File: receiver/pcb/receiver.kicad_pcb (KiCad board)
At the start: 4 copper layers, 41 x 41 mm, 25 parts, among them U1 RZ7886, U2 RZ7886, U3 XIAO ESP32C3

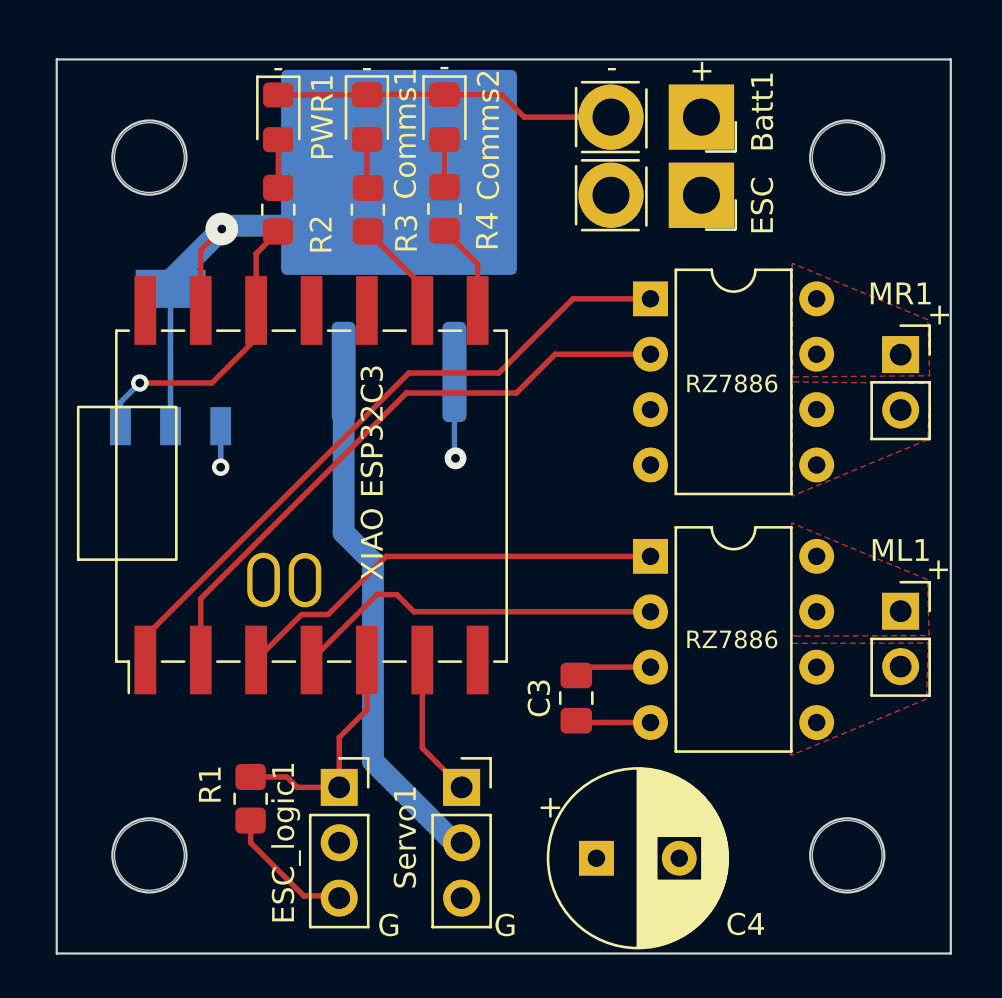
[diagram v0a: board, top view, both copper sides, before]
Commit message: fixed mistakenly small motor pads in receiver V6.
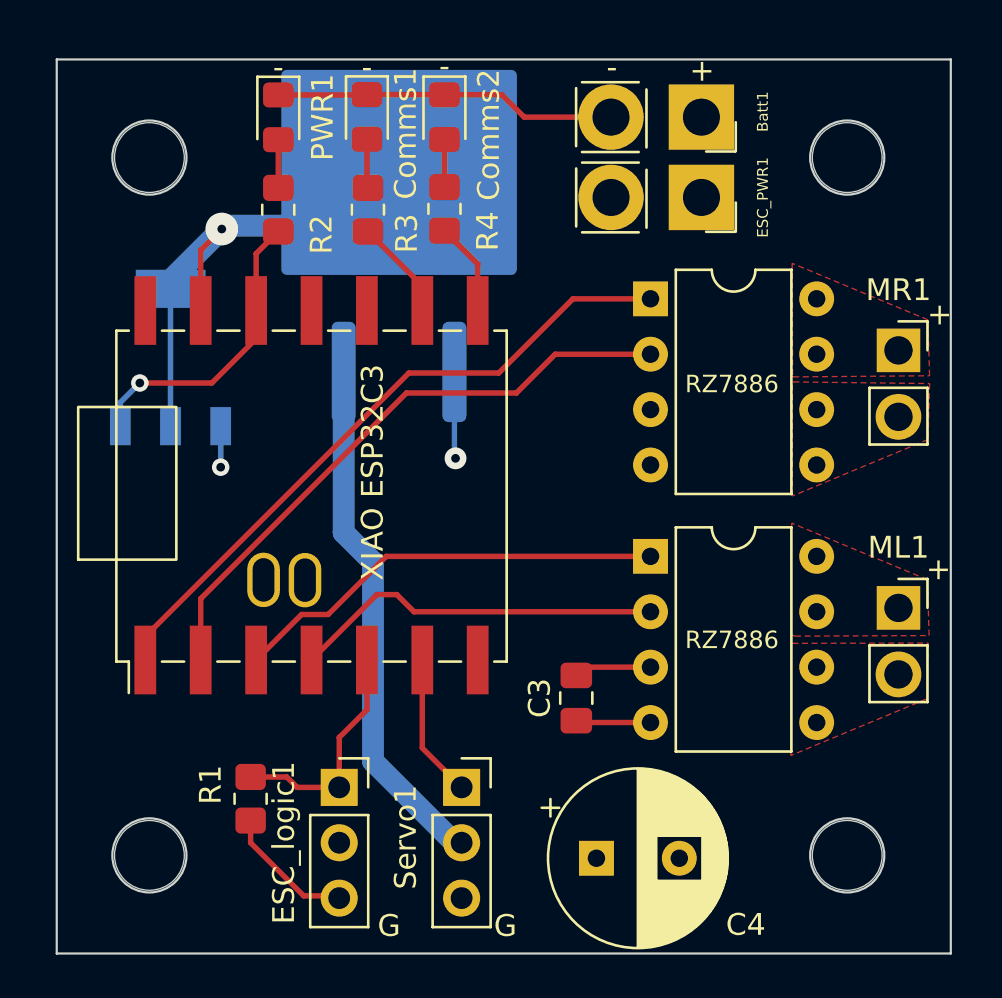
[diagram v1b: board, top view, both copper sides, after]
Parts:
- removed ESC: Conn_01x02_Female, custom:battery_pads
- added ESC_PWR1: Conn_01x02_Female, custom:battery_pads, F.Cu at (174.8, 84.8)
- ML1: footprint Connector_PinSocket_2.54mm:PinSocket_1x02_P2.54mm_Vertical -> custom:DC_motor_output
- MR1: value Conn_01x02_Female -> motor_output; footprint Connector_PinSocket_2.54mm:PinSocket_1x02_P2.54mm_Vertical -> custom:DC_motor_output
- moved MR1 0.22 mm to (185.1, 91.8)
- moved ML1 0.18 mm to (185.1, 103.7)
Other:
- board text added: "VS Receiver V7"
- board text removed: "VS Receiver V6"

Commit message: V8 as ordered from jlcpcb. Order #: Y34-2569843A
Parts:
- removed C3: .1 uF, Capacitor_SMD:C_0805_2012Metric_Pad1.18x1.45mm_HandSolder
- removed C4: 470 uF, Capacitor_THT:CP_Radial_D8.0mm_P3.80mm
- removed L7806: L7806, Package_TO_SOT_SMD:TO-263-2_TabPin1
- removed U2: RZ7886, Package_DIP:DIP-8_W7.62mm
- removed U3: XIAO ESP32C3, XIAO_ESP32C3:xiao_esp32c3
- added C1: 270 uF, Capacitor_THT:CP_Radial_D8.0mm_P3.80mm, F.Cu at (170.0, 114.7)
- added C2: 100nF, Capacitor_SMD:C_0805_2012Metric_Pad1.18x1.45mm_HandSolder, F.Cu at (167.9, 83.6)
- added IC1: L7806CD2T-TR, L7806CD2T-TR:TO254P1542X460-3N, B.Cu at (162.3, 87.7)
- added ML2: VNH7100BASTR, VNH7100BASTR:SOIC127P600X175-16N, F.Cu at (179.3, 105.4)
- added ML_selector1: ML_selector, Connector_PinSocket_2.54mm:PinSocket_1x03_P2.54mm_Vertical, F.Cu at (172.2, 106.1)
- added MR2: VNH7100BASTR, VNH7100BASTR:SOIC127P600X175-16N, F.Cu at (179.3, 92.5)
- added MR_selector1: MR_selector, Connector_PinSocket_2.54mm:PinSocket_1x03_P2.54mm_Vertical, F.Cu at (172.6, 95.5)
- U1: value RZ7886 -> XIAO ESP32C3; footprint Package_DIP:DIP-8_W7.62mm -> XIAO_ESP32C3:xiao_esp32c3
- moved U1 15.9 mm to (160.0, 97.5), turned to 90 degrees
- moved MR1 1.04 mm to (185.3, 90.8)
- moved ML1 0.39 mm to (185.5, 103.5)
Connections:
- R3 pad 1: Net-(U3-D8) -> Net-(U1-D8)
- R4 pad 1: Net-(U3-D7) -> Net-(U1-D6)
- U1 pad 3: GND -> Net-(ML2-INB)
- U1 pad 4: +12V -> Net-(ML2-INA)
- U1 pad 5: Net-(MR1-Pin_2) -> Net-(ESC_logic1-Pin_1)
- U1 pad 6: Net-(MR1-Pin_2) -> Net-(Servo1-Pin_1)
- U1 pad 7: Net-(MR1-Pin_1) -> Net-(U1-D6)
- U1 pad 8: Net-(MR1-Pin_1) -> /MR_PWM
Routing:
- net Net-(U1-D6): track 0.00 -> 72.9 mm
- net /ML_PWM: track 0.00 -> 33.7 mm, vias 0 -> 2
- net Net-(ML2-INB): track 0.00 -> 26.9 mm
- net /MR_sense: track 0.00 -> 25.6 mm, vias 0 -> 2
- net GND: track 50.3 -> 74.6 mm, vias 1 -> 11
- net /MR_PWM: track 0.00 -> 22.4 mm, vias 0 -> 2
- net Net-(ML2-INA): track 0.00 -> 21.0 mm
- net Net-(U2-BI): track 20.1 -> 0.00 mm
- net +12V: track 9.30 -> 28.5 mm, vias 2 -> 8
- net Net-(U2-FI): track 17.1 -> 0.00 mm
- net Net-(MR2-SEL0): track 0.00 -> 11.5 mm, vias 0 -> 1
- net Net-(ML2-SEL0): track 0.00 -> 11.2 mm, vias 0 -> 1
- net Net-(MR2-INB): track 30.7 -> 36.1 mm
- net Net-(MR2-INA): track 28.1 -> 33.3 mm
- net Net-(U3-D8): track 4.66 -> 0.00 mm
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- added copper zone on F.Cu, net GND
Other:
- board text added: "VS Receiver V8"
- board text removed: "VS Receiver V7"

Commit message: V9 ready to order
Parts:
- removed H1, H2, H3, H4: MountingHole, MountingHole:MountingHole_3.2mm_M3
- removed ML_selector1: ML_selector, Connector_PinSocket_2.54mm:PinSocket_1x03_P2.54mm_Vertical
- removed MR_selector1: MR_selector, Connector_PinSocket_2.54mm:PinSocket_1x03_P2.54mm_Vertical
- ML1, ML2, MR1, MR2: moved to B.Cu
- moved C1 37.3 mm to (150.4, 83.0)
- moved Servo1 31.3 mm to (168.2, 80.7), turned to 90 degrees
- moved ESC_logic1 28.8 mm to (168.2, 84.5), turned to 90 degrees
- moved R1 28.5 mm to (172.8, 89.8), turned to -90 degrees
- moved PWR1 26.5 mm to (172.8, 102.2), turned to 90 degrees
- moved R2 21.2 mm to (169.5, 102.2), turned to -90 degrees
- moved Comms1 20.7 mm to (172.8, 98.0), turned to 90 degrees
- moved R3 15.3 mm to (169.5, 98.0), turned to -90 degrees
- moved Comms2 15.2 mm to (172.8, 93.8), turned to 90 degrees
- moved PS1 12.8 mm to (150.5, 104.9), turned to -90 degrees
- moved Batt1 11.8 mm to (163.0, 81.1)
- moved ESC_PWR1 11.8 mm to (163.0, 84.8)
- moved ML1 10.2 mm to (175.5, 101.7), turned to 180 degrees
- moved R4 10.1 mm to (169.5, 94.0), turned to -90 degrees
- moved ML2 10.0 mm to (169.5, 103.5), turned to 180 degrees
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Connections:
- ML2 pad 14: Net-(ML2-SEL0) -> unconnected-(ML2-SEL0-Pad14)
- MR2 pad 14: Net-(MR2-SEL0) -> unconnected-(MR2-SEL0-Pad14)
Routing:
- net Net-(U1-D6): track 72.9 -> 21.5 mm
- net Net-(Servo1-Pin_1): track 6.59 -> 51.2 mm
- net Net-(ESC_logic1-Pin_1): track 10.6 -> 41.8 mm, vias 0 -> 3
- net GND: track 74.6 -> 96.3 mm, vias 11 -> 10
- net +3V3: track 13.9 -> 32.6 mm, vias 1 -> 2
- net /MR_sense: track 25.6 -> 7.25 mm, vias 2 -> 1
- net /MR_PWM: track 22.4 -> 8.05 mm, vias 2 -> 1
- net /ML_PWM: track 33.7 -> 19.4 mm, vias 2 -> 1
- net Net-(MR2-SEL0): track 11.5 -> 0.00 mm, vias 1 -> 0
- net Net-(ML2-SEL0): track 11.2 -> 0.00 mm, vias 1 -> 0
- net Net-(ML1-Pin_2): track 0.04 -> 9.51 mm, vias 0 -> 1
- net Net-(U1-D8): track 4.66 -> 12.8 mm
- net Net-(ML2-INB): track 26.9 -> 19.0 mm, vias 0 -> 3
- net Net-(MR2-INB): track 36.1 -> 29.7 mm, vias 0 -> 3
- net Net-(Comms2-A): track 2.18 -> 8.11 mm
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- added copper zone on B.Cu, net Net-(ML1-Pin_1)
- added copper zone on B.Cu, net Net-(ML1-Pin_2)
- added copper zone on B.Cu, net Net-(MR1-Pin_1)
- added copper zone on B.Cu, net Net-(MR1-Pin_2)
- removed copper zone on F.Cu, net GND
- removed copper zone on F.Cu, net Net-(ML1-Pin_1)
- removed copper zone on F.Cu, net Net-(ML1-Pin_2)
- removed copper zone on F.Cu, net Net-(MR1-Pin_1)
- removed copper zone on F.Cu, net Net-(MR1-Pin_2)
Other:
- board size 41 x 41 mm -> 31.5 x 31 mm
- board text added: "VS Receiver V9"
- board text removed: "32x32mm mounting holes"
- board text removed: "VS Receiver V8"
